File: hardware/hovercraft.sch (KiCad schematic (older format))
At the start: 9 parts, among them J1 USB_OTG, U1 ATMEGA32U2-AU, Y1 Crystal_GND24

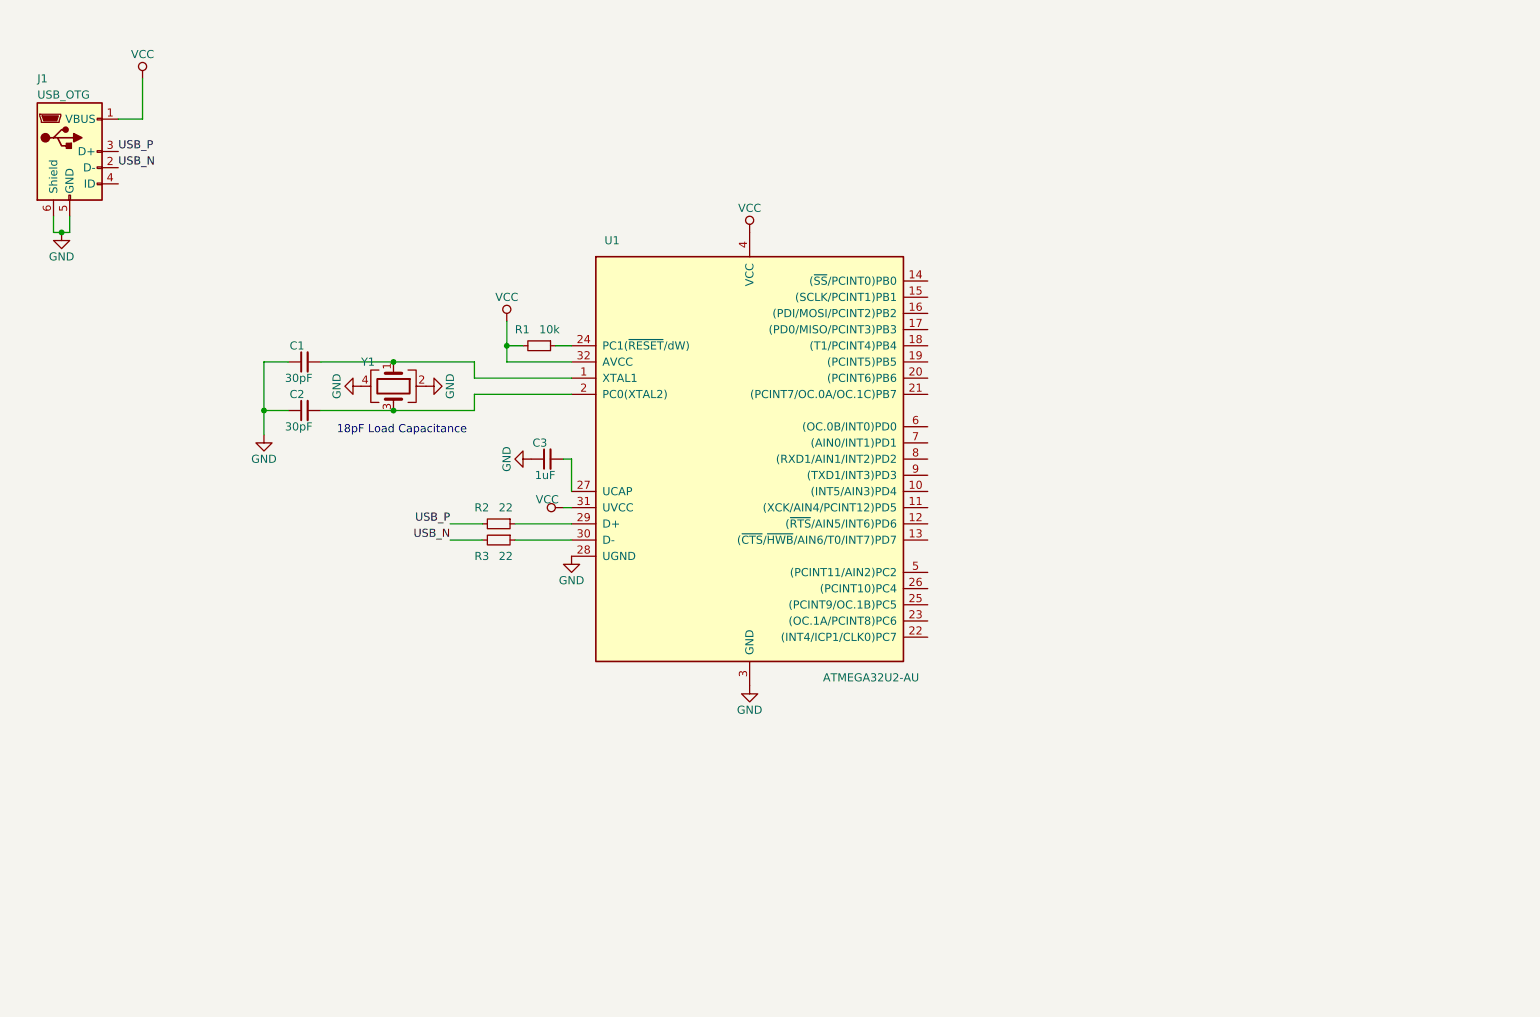
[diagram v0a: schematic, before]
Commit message: Filled out the schematic with servo and power connectors and populated these on the PCB
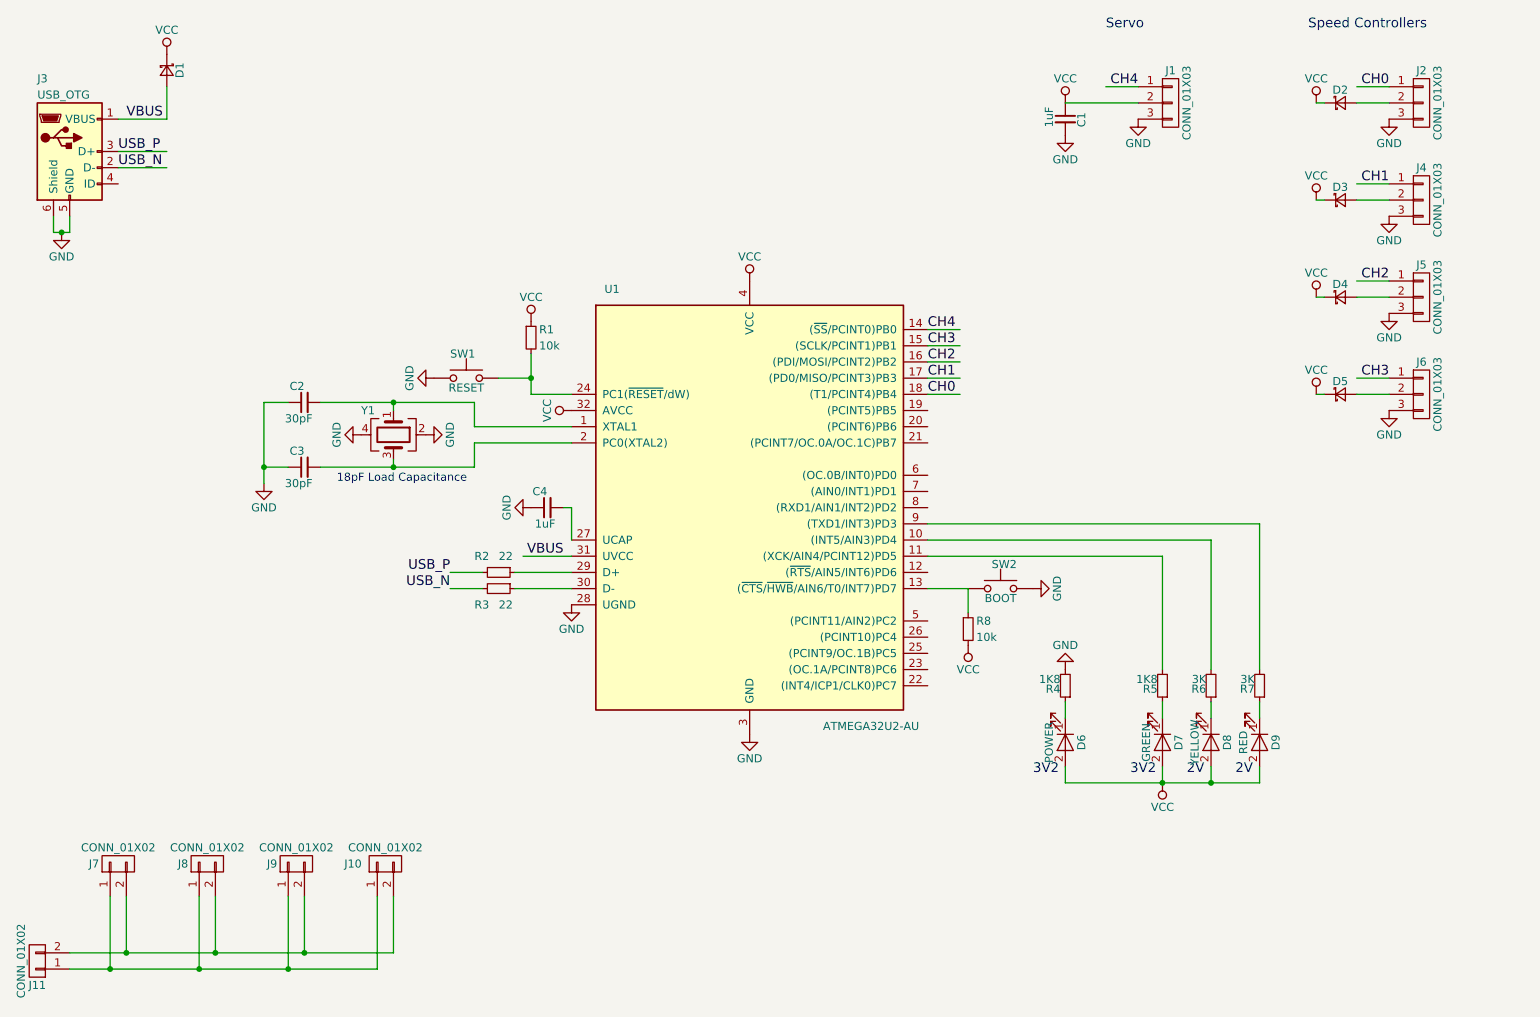
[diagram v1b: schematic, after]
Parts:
- added C1: 1uF, Capacitors_SMD:C_0603, symbol C_Small
- added D1, D2, D3, D4, D5: D_Schottky_Small, Diodes_SMD:D_SMA, symbol D_Schottky_Small
- added D6: POWER, LEDs:LED_0603, symbol LED
- added D7: GREEN, LEDs:LED_0603, symbol LED
- added D8: YELLOW, LEDs:LED_0603, symbol LED
- added D9: RED, LEDs:LED_0603, symbol LED
- added J1, J2, J4, J5, J6: CONN_01X03, Pin_Headers:Pin_Header_Angled_1x03_Pitch2.54mm, symbol CONN_01X03
- added J10, J11, J7, J8, J9: CONN_01X02, modules:XT60, symbol CONN_01X02
- added R4, R5: 1K8, Resistors_SMD:R_0603, symbol R_Small
- added R6, R7: 3K, Resistors_SMD:R_0603, symbol R_Small
- added R8: 10k, Resistors_SMD:R_0603, symbol R_Small
- added SW1: RESET, Buttons_Switches_SMD:Panasonic_EVQPUJ_EVQPUA, symbol SW_Push
- added SW2: BOOT, Buttons_Switches_SMD:Panasonic_EVQPUJ_EVQPUA, symbol SW_Push
- renumbered C1 to C2, C2 to C3, C3 to C4, J1 to J3
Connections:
- net labels added: CH0, CH1, CH2, CH3, CH4, VBUS
- wire segments 25 -> 74
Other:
- note added: "2V"
- note added: "3V2"
- note added: "Servo"
- note added: "Speed Controllers"
- moved on the sheet: C2, C3, C4, R1, R2, R3, U1, Y1

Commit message: Add the HC-12 serial radio module to the component library
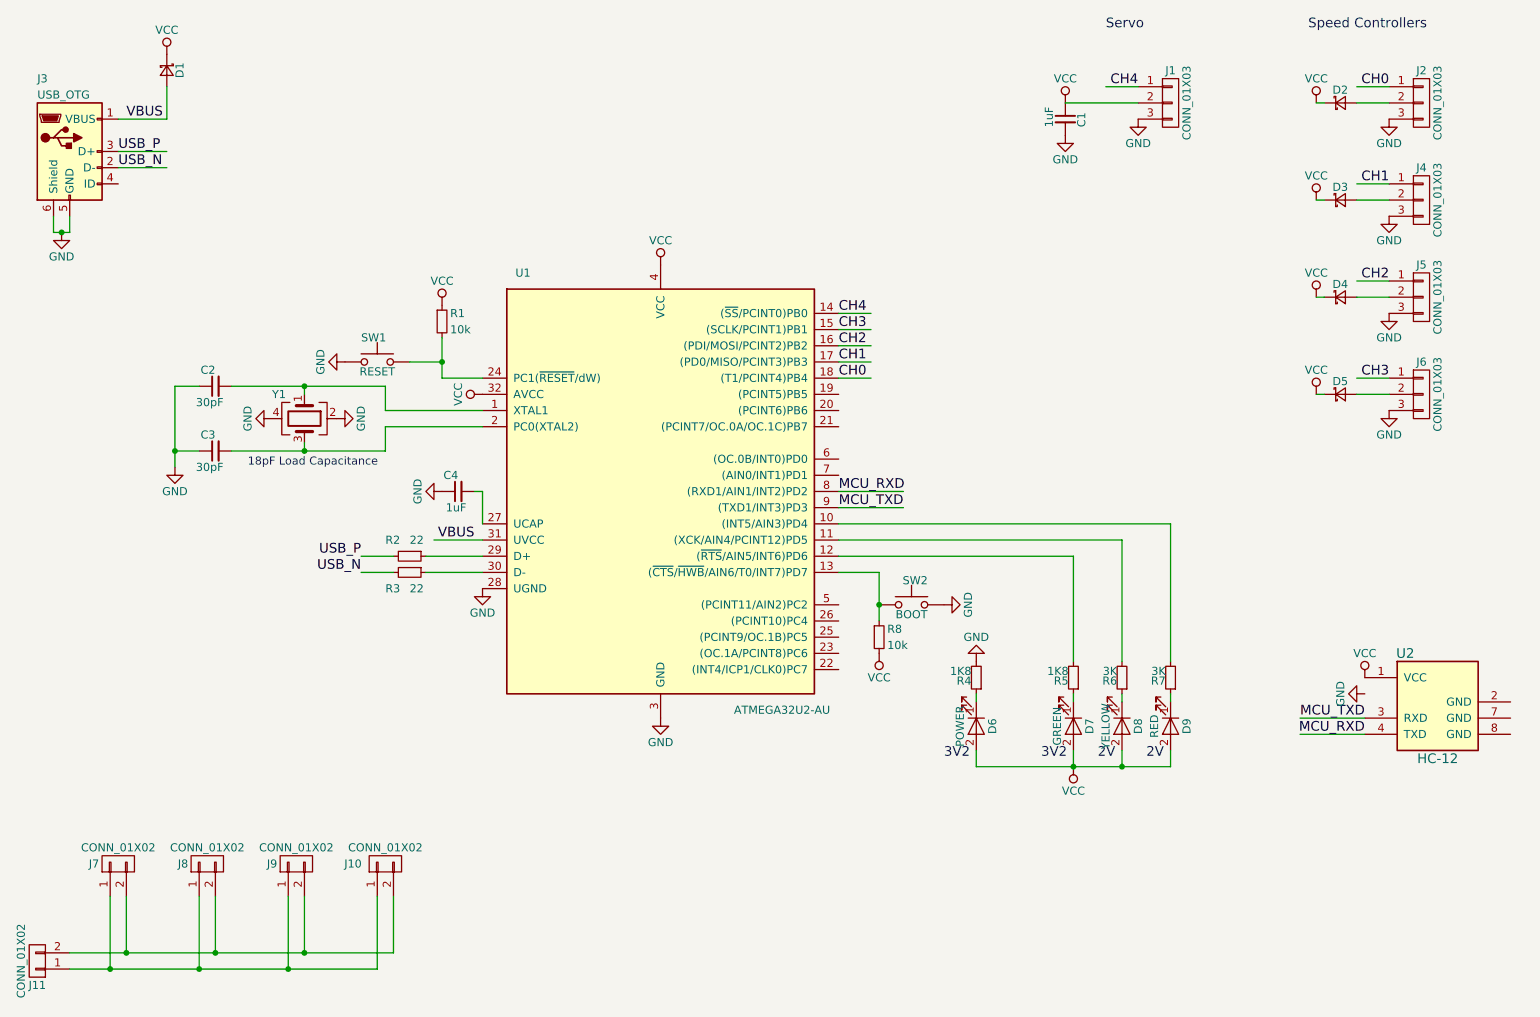
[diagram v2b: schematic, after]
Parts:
- added U2: HC-12, symbol HC-12
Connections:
- net labels added: MCU_RXD, MCU_TXD
- wire segments 74 -> 78
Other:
- moved on the sheet: C2, C3, C4, D6, D7, D8, D9, R1, R2, R3, R4, R5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

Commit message: Add the HC-12 foot print and repopulate the board to fit it in.
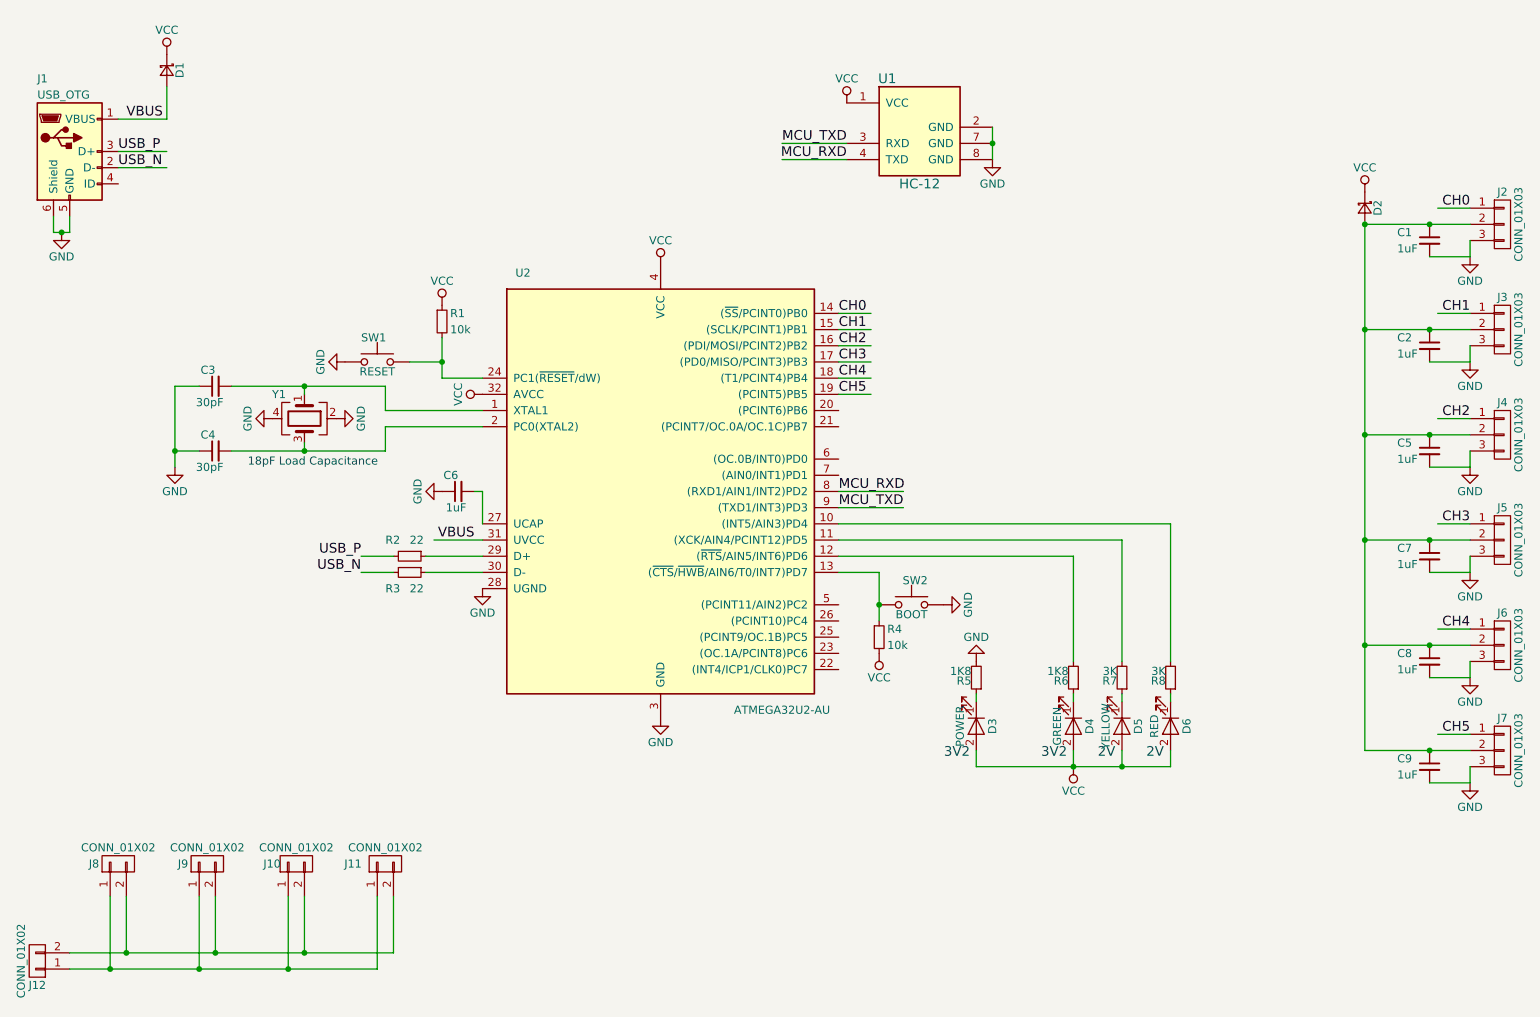
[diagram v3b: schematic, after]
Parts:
- removed D3, D4, D5: D_Schottky_Small, Diodes_SMD:D_SMA, symbol D_Schottky_Small
- removed J1: CONN_01X03, Pin_Headers:Pin_Header_Angled_1x03_Pitch2.54mm, symbol CONN_01X03
- added C2, C5, C7, C8, C9: 1uF, Capacitors_SMD:C_0603, symbol C_Small
- added J3, J7: CONN_01X03, Pin_Headers:Pin_Header_Angled_1x03_Pitch2.54mm, symbol CONN_01X03
- U1: renamed from U2; footprint (none) -> modules:HC-12
- renumbered C2 to C3, C3 to C4, C4 to C6, D6 to D3, D7 to D4, D8 to D5, D9 to D6, J3 to J1, J9 to J10, J10 to J11, J11 to J12, J7 to J8, J8 to J9, R8 to R4, R4 to R5, R5 to R6, R6 to R7, R7 to R8, U1 to U2
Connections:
- net labels added: CH5
- wire segments 78 -> 91
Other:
- note removed: "Servo"
- note removed: "Speed Controllers"
- moved on the sheet: C1, J2, U1
